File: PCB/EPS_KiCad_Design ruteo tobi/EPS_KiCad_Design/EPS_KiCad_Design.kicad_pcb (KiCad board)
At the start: 4 copper layers, 90 x 90.2 mm, 133 parts, among them IC1 INA226AIDGST, IC10 TPS2553QDBVRQ1, IC11 INA226AIDGST, IC2 TPS2553QDBVRQ1, IC3 INA226AIDGST, IC4 TPS2553QDBVRQ1, IC5 AP63205WU-7, IC6 STM32L433CBT7, IC7 LT3652IMSE#PBF, IC8 INA226AIDGST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

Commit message: Cambios menores
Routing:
- net 3V3_1: track 230.3 -> 220.6 mm
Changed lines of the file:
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@@
 		(tags "capacitor handsolder")
 		(property "Reference" "C6"
-			(at -2.94 0.01 0)
+			(at -2.7875 0.1 0)
 			(layer "F.SilkS")
 			(effects
@@
 		(sheetname "/MCU/")
 		(sheetfile "MCU.kicad_sch")
+		(clearance 0.12)
 		(attr through_hole)
 		(fp_line
@@
 		(tags "capacitor handsolder")
 		(property "Reference" "C7"
-			(at -3.0325 0.02 0)
+			(at -2.7775 -0.01 0)
 			(layer "F.SilkS")
 			(effects
@@
 	)
 	(segment
-		(start 168.1 133.5)
-		(end 168.1 134.3625)
+		(start 167 136.55)
+		(end 167 136.5625)
 		(width 0.6)
 		(layer "F.Cu")
@@
 	)
 	(segment
-		(start 166.0375 136.5625)
-		(end 167.0125 136.5625)
+		(start 168.1 133.5)
+		(end 168.1 134.3625)
 		(width 0.6)
 		(layer "F.Cu")
@@
 	)
 	(segment
-		(start 133.8 134.6625)
-		(end 133.8 114.9)
+		(start 167.875 127.8)
+		(end 167.875 129.125)
 		(width 0.6)
 		(layer "F.Cu")
@@
 	)
 	(segment
-		(start 166.0375 136.5625)
-		(end 131.9 136.5625)
+		(start 133.8 134.6625)
+		(end 133.8 114.9)
 		(width 0.6)
 		(layer "F.Cu")
@@
 	)
 	(segment
-		(start 170.3 136.5625)
-		(end 176.7875 136.5625)
-		(width 0.6)
-		(layer "F.Cu")
-		(net 15)
-	)
-	(segment
 		(start 134.83 113.87)
 		(end 135.565 113.87)
@@
 	)
 	(segment
-		(start 167.0125 136.5625)
-		(end 176.7875 136.5625)
-		(width 0.6)
-		(layer "F.Cu")
-		(net 15)
-	)
-	(segment
-		(start 167.875 129.125)
-		(end 165.4 131.6)
-		(width 0.6)
-		(layer "F.Cu")
-		(net 15)
-	)
-	(segment
 		(start 173.6 111)
 		(end 175.6 111)
@@
 	)
 	(segment
-		(start 167.875 127.8)
-		(end 167.875 129.125)
+		(start 167.875 129.125)
+		(end 165.4 131.6)
 		(width 0.6)
 		(layer "F.Cu")
@@
 	)
 	(segment
-		(start 167.0125 136.5625)
-		(end 170.3 136.5625)
-		(width 0.6)
-		(layer "F.Cu")
-		(net 15)
-	)
-	(segment
 		(start 186.55 121.7)
 		(end 182.25 126)
@@
 	)
 	(segment
+		(start 165.4 131.6)
+		(end 165.4 134.95)
+		(width 0.6)
+		(layer "F.Cu")
+		(net 15)
+	)
+	(segment
 		(start 152.3 87.85)
 		(end 150.35 85.9)
@@
 	)
 	(segment
-		(start 167 136.55)
-		(end 167 136.5625)
-		(width 0.6)
-		(layer "F.Cu")
-		(net 15)
-	)
-	(segment
 		(start 186.55 115)
 		(end 184.038 117.512)
@@
 	)
 	(segment
-		(start 165.4 131.6)
-		(end 165.4 134.95)
-		(width 0.6)
-		(layer "F.Cu")
-		(net 15)
-	)
-	(segment
 		(start 177.3 124.5)
 		(end 177.3 125.7)
@@
 	)
 	(segment
+		(start 131.9 136.5625)
+		(end 176.7875 136.5625)
+		(width 0.6)
+		(layer "F.Cu")
+		(net 15)
+	)
+	(segment
 		(start 150.35 85.9)
 		(end 149.05 85.9)
@@
 	)
 	(segment
-		(start 165.4 134.95)
-		(end 167.0125 136.5625)
-		(width 0.6)
-		(layer "F.Cu")
-		(net 15)
-	)
-	(segment
 		(start 131.9 136.5625)
 		(end 122.7 136.5625)
@@
 		(layer "F.Cu")
 		(net 15)
+	)
+	(segment
+		(start 165.4 134.95)
+		(end 167 136.55)
+		(width 0.6)
+		(layer "F.Cu")
+		(net 15)

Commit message: Actualizacion del PCB
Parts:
- C15, C16: value 8.2pF -> 6.8pF
- L1, L4: footprint SRR4528A-3R9Y_Footprint:SRR4528A3R9Y -> ASPI:ASPI0628150MT1
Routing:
- net GND: vias 260 -> 214

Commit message: Estapadines agregados en el diseño
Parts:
- J2: value FTSH-107-01-L-D-K -> Conn_01x05; footprint FTSH-107-01-L-D-K_Footprint:FTSH-107-XX-YYY-D-K -> TSM_Connector:TSM10501LSV
- moved C19 20.3 mm to (198.9, 126.5)
- moved C20 20.3 mm to (198.9, 128.6)
- moved C22 20.3 mm to (198.9, 137.0)
- moved C23 20.3 mm to (198.9, 134.9)
- moved C24 20.3 mm to (198.9, 130.7)
- moved C25 20.3 mm to (198.9, 132.8)
- moved J2 5.38 mm to (172.2, 134.3)
- moved C21 2.52 mm to (149.4, 128.2)
- moved S1 2.52 mm to (156.4, 128.3)
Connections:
- IC6 pad 12: /MCU/PA2 -> unconnected-(IC6-PA2-Pad12)
- IC6 pad 13: /MCU/PA3 -> unconnected-(IC6-PA3-Pad13)
- IC6 pad 39: /MCU/PB3 -> unconnected-(IC6-PB3-Pad39)
- J2 pad 1: unconnected-(J2-Pad1) -> 3V3_1
- J2 pad 2: unconnected-(J2-Pad2) -> /MCU/PA13
- J2 pad 3: 3V3_1 -> /MCU/PA14
- J2 pad 4: /MCU/PA13 -> GND
- J2 pad 5: GND -> /MCU/NRST
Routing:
- net /MCU/PB3: track 32.8 -> 0.00 mm, vias 2 -> 0
- net /MCU/PA3: track 11.6 -> 0.00 mm
- net /MCU/PA2: track 10.9 -> 0.00 mm
- net /MCU/PA13: track 29.0 -> 20.3 mm
- net GND: track 67.6 -> 59.7 mm, vias 214 -> 208
- net 3V3_1: track 220.6 -> 215.1 mm
- net /MCU/PA14: track 31.3 -> 27.7 mm
- net /MCU/NRST: track 24.1 -> 25.2 mm, vias 2 -> 0

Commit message: cambios en el ruteo
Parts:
- added C46: 100nF, Capacitor_SMD:C_0805_2012Metric_Pad1.18x1.45mm_HandSolder, B.Cu at (105.0, 63.6)
- added C47: 100nF, Capacitor_SMD:C_0805_2012Metric_Pad1.18x1.45mm_HandSolder, B.Cu at (185.0, 63.5)
- added C48: 100nF, Capacitor_SMD:C_0805_2012Metric_Pad1.18x1.45mm_HandSolder, B.Cu at (185.0, 132.2)
- added C49: 100nF, Capacitor_SMD:C_0805_2012Metric_Pad1.18x1.45mm_HandSolder, B.Cu at (105.0, 131.9)
- C19, C20, C22, C23, C24, C25, C26, C27, C28, FB1: moved to B.Cu
- H1, H2, H3, H4: value MountingHole -> MountingHole_Pad
- moved C19 32.2 mm to (169.2, 114.1), turned to 180 degrees
- moved C20 32.2 mm to (169.2, 116.2), turned to 180 degrees
- moved C25 27.2 mm to (179.8, 113.5)
- moved C24 24.4 mm to (179.8, 115.6)
- moved C22 22.5 mm to (179.3, 126.0)
- moved C23 20.8 mm to (179.3, 128.1)
- moved C26 5.82 mm to (169.5, 127.1)
- moved C17 5.63 mm to (159.8, 120.8)
- moved C18 5.63 mm to (159.8, 124.9)
- moved R11 5.63 mm to (168.2, 123.8)
- moved Y2 5.63 mm to (164.4, 122.9)
- moved C27 3.96 mm to (169.5, 122.9)
- moved C21 3.76 mm to (151.6, 131.2)
- moved S1 3.76 mm to (158.6, 131.4)
- moved C28 2.67 mm to (169.5, 125.0)
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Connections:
- H1 pad 1: (no net) -> Net-(C48-Pad2)
- H2 pad 1: (no net) -> Net-(C47-Pad1)
- H3 pad 1: (no net) -> Net-(C49-Pad2)
- H4 pad 1: (no net) -> Net-(C46-Pad1)
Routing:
- net SCL: track 175.3 -> 187.4 mm
- net GND: track 59.7 -> 71.6 mm, vias 208 -> 222
- net 3V3_1: track 215.1 -> 226.5 mm, vias 2 -> 6
- net /MCU/PH0: track 15.1 -> 10.1 mm
- net Net-(C49-Pad2): track 0.00 -> 4.91 mm
- net Net-(C48-Pad2): track 0.00 -> 4.71 mm
- net Net-(C46-Pad1): track 0.00 -> 4.66 mm
- net Net-(C47-Pad1): track 0.00 -> 4.61 mm
- net /MCU/PH1: track 7.20 -> 4.29 mm
- net /MCU/NRST: track 25.2 -> 22.8 mm
- net SDA OBC: track 105.7 -> 107.2 mm
- net ALERT: track 165.5 -> 166.9 mm
- net /MCU/PA14: track 27.7 -> 26.4 mm
- net 5V_OCP: track 7.69 -> 7.02 mm
- net SDA: track 189.8 -> 190.0 mm, vias 6 -> 7
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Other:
- board text added: "3V3"
- board text added: "BAT"
- board text added: "DP1"
- board text added: "DP2"
- board text added: "FUENTE"
- board text added: "GND"
- board text added: "NOREG"
- board text added: "NRST"
- board text added: "PANEL"
- board text added: "SWCLK"
- board text added: "SWDIO"
- board text added: "TEMP"

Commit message: Cambios pcb
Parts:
- moved D3 2.14 mm to (113.9, 81.3)
- moved C46 1.23 mm to (105.0, 64.8)
- moved D4 0.85 mm to (115.3, 92.9)
- moved S2 0.74 mm to (170.0, 107.4)
- moved SD12-01FTG2 0.63 mm to (139.8, 127.9)
- moved C47 0.47 mm to (185.0, 64.0)
- moved LED4 0.42 mm to (142.1, 125.8)
- moved R29 0.41 mm to (138.2, 125.8)
- moved SD12-01FTG1 0.23 mm to (111.8, 122.8)
- moved J9 0.21 mm to (142.9, 132.4)
- moved C37 0.19 mm to (140.1, 122.3)
- moved J3 0.15 mm to (107.5, 130.7)
- moved C30 0.08 mm to (113.9, 122.8)
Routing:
- net GPIO3: track 89.1 -> 94.3 mm
- net GPIO5: track 78.9 -> 74.8 mm
- net GPIO4: track 84.9 -> 88.9 mm
- net Net-(C47-Pad1): track 4.61 -> 7.49 mm
- net GPIO6: track 86.7 -> 84.2 mm
- net GPIO1: track 69.0 -> 71.5 mm
- net Net-(D3-A): track 6.36 -> 8.57 mm
- net 3V3_1: track 226.5 -> 228.1 mm
- net GPIO2: track 67.2 -> 68.5 mm
- net Net-(C46-Pad1): track 4.66 -> 3.51 mm
- net Net-(S2-COM): track 6.47 -> 7.23 mm
- net /MPPT + BATTERY CHARGER/IN-: track 37.9 -> 38.5 mm
- net GND: track 71.6 -> 71.9 mm, vias 222 -> 254
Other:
- board text added: "BOOT"
- board text added: "RST"

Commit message: cambios minimos para pasar el DFM Checker
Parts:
- C46, C47, C48, C49: moved to F.Cu
- moved C49 8.40 mm to (113.4, 132.7), turned to 180 degrees
- moved C47 2.51 mm to (185.0, 66.5)
- moved C48 1.89 mm to (185.1, 130.3)
- moved C46 1.70 mm to (104.9, 66.5)
- moved S2 1.59 mm to (170.0, 105.8)
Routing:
- net GND: track 71.9 -> 77.0 mm, vias 254 -> 257
- net Net-(C46-Pad1): track 3.51 -> 7.62 mm
- net Net-(C49-Pad2): track 4.91 -> 7.06 mm
- net Net-(S2-COM): track 7.23 -> 8.79 mm
- net 3V3_1: track 228.1 -> 229.3 mm

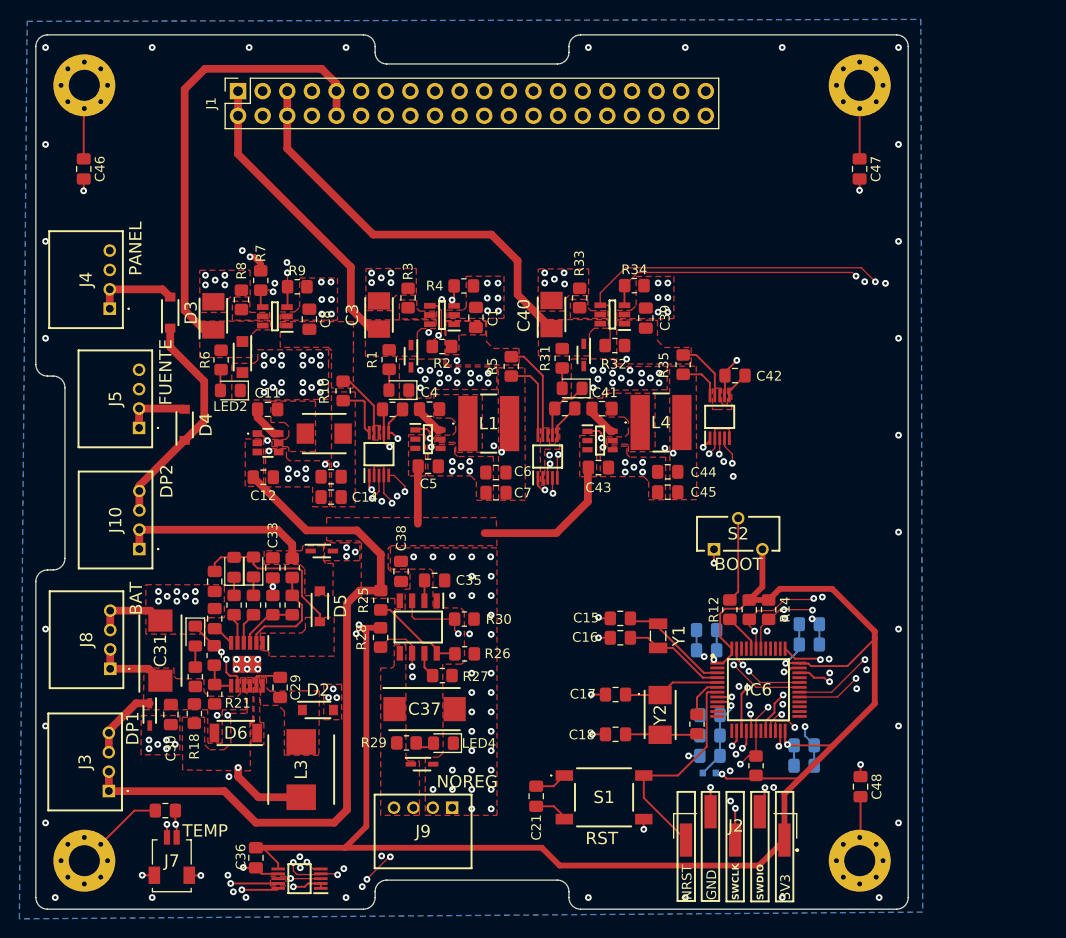
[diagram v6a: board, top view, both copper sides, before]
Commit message: Agrege nombres visibles a PC104
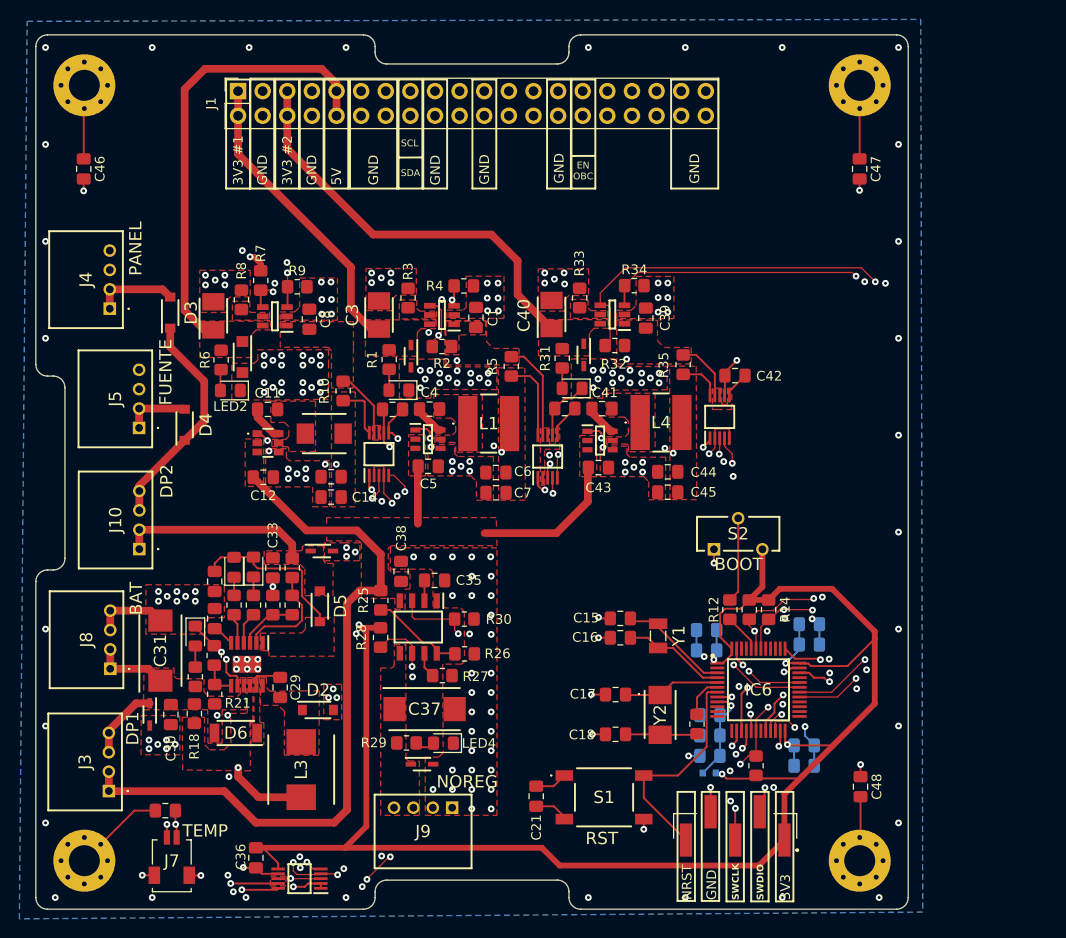
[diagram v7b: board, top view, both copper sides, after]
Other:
- board text added: "3V3 #1"
- board text added: "3V3 #2"
- board text added: "5V"
- board text added: "EN OBC"
- board text added: "SCL"
- board text added: "SDA"
